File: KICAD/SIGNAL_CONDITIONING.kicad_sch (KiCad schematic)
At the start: 59 parts, among them U1 LM358, U4 LM358, U5 LM358, U6 LM358, U8 TLV9061

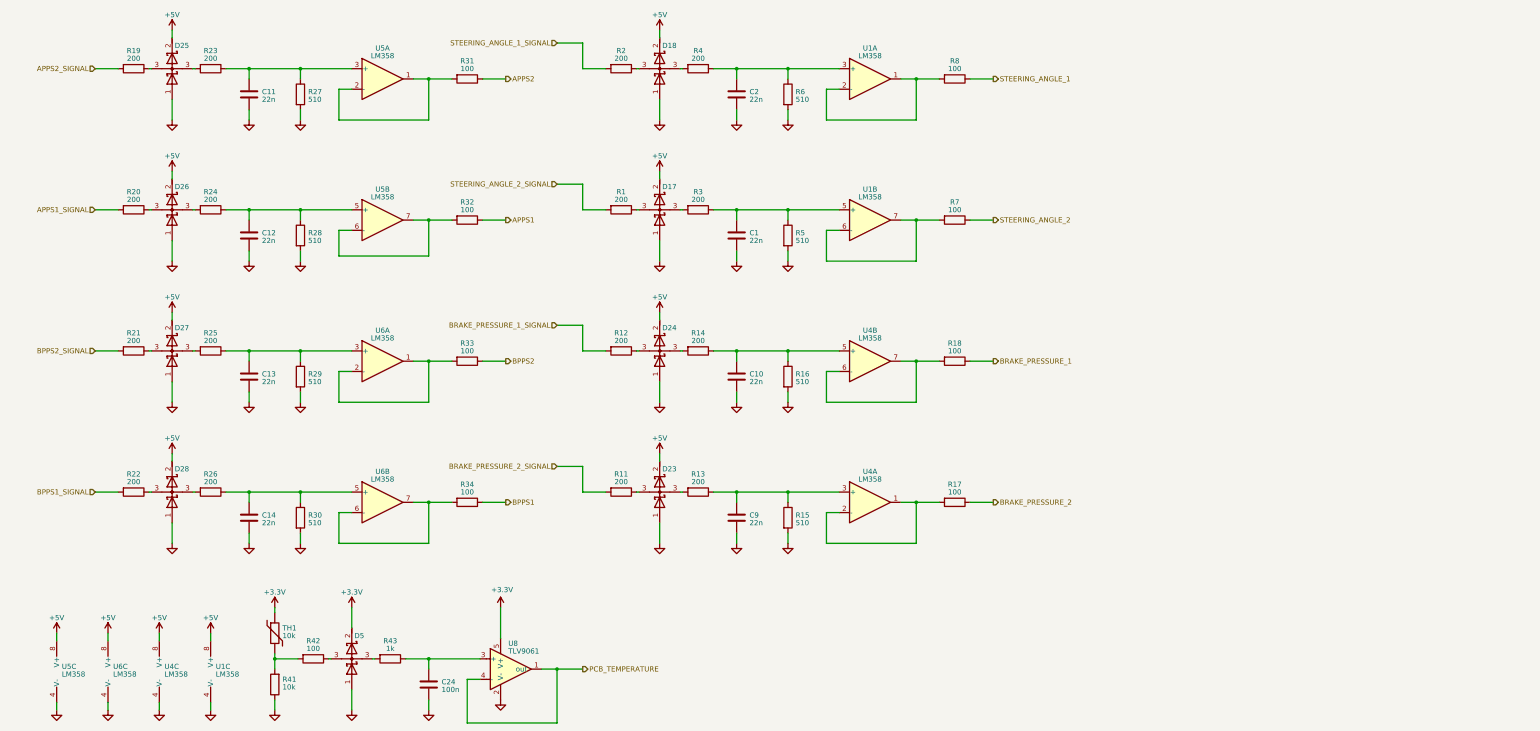
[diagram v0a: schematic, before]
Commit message: SIGNAL_CONDITIONING
Ändrat signal pins och dess output pins till ANALOG_SIGNAL_1 - ANALOG_1 osv för alla adnra siffror upp till 12. Pratade med VIktor ocg de vill att vi har tolv analoga inpus. Vi ska även döpa alla inuts till just ANALOG N (N-siffra) för att VMUn ska vara flexibel i framtiden och kunna användas för olika analoga sensorer utan att signalerna har angivna namn. Kopierade in fyra signal konditionerare till då det innan endast fanns 8 (eller 9) nu finns 12 (kanske 13)
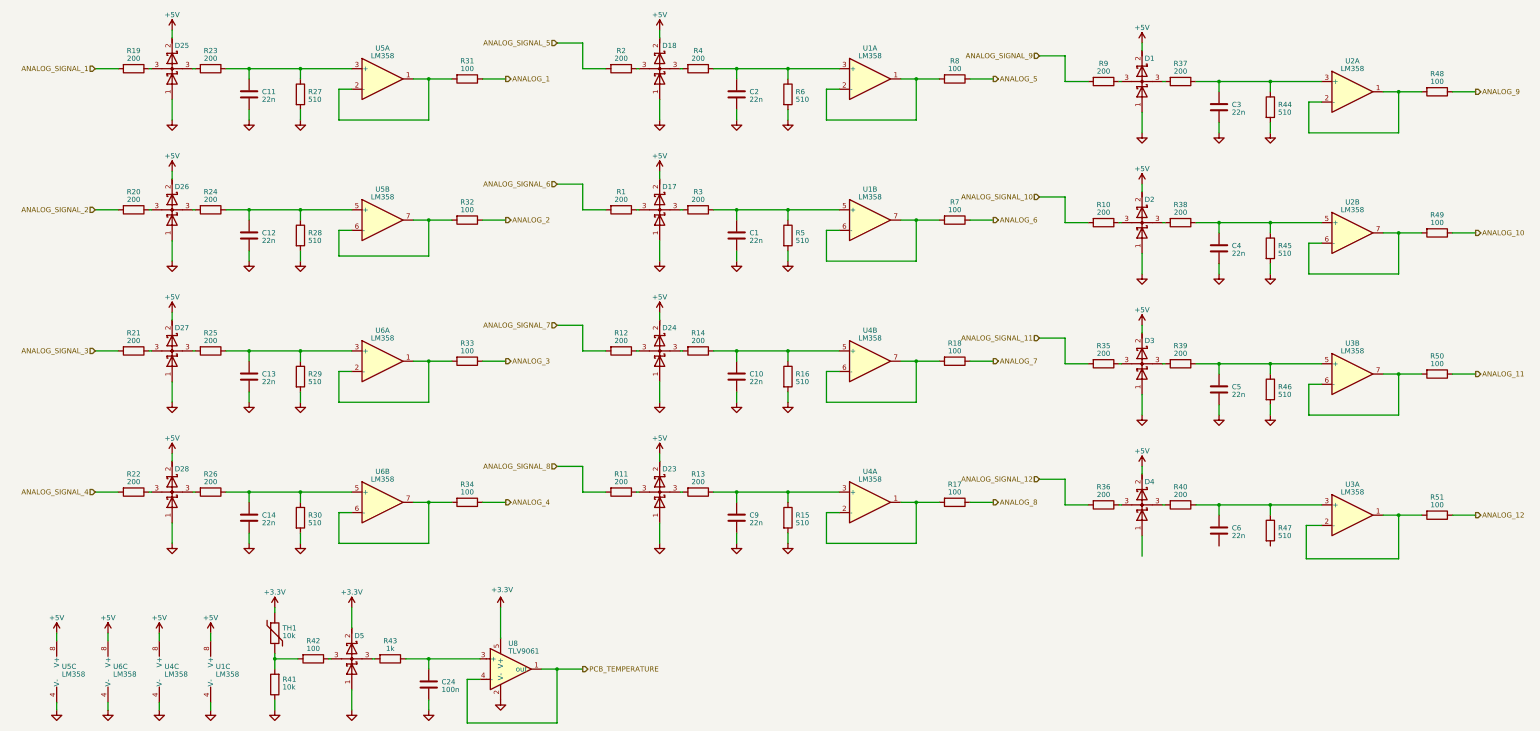
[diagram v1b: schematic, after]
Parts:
- added C3, C4, C5, C6: 22n, Capacitor_SMD:C_0603_1608Metric, symbol Device:C
- added D1, D2, D3, D4: D_Schottky_x2_Serial_AKC, Package_TO_SOT_SMD:SOT-23, symbol KTHFS:D_Schottky_x2_Serial_AKC
- added R10, R35, R36, R37, R38, R39, R40, R9: 200, Resistor_SMD:R_0603_1608Metric, symbol Device:R
- added R44, R45, R46, R47: 510, Resistor_SMD:R_0603_1608Metric, symbol Device:R
- added R48, R49, R50, R51: 100, Resistor_SMD:R_0603_1608Metric, symbol Device:R
- added U2, U3: LM358, Package_SO:SOIC-8_3.9x4.9mm_P1.27mm, symbol Amplifier_Operational:LM358
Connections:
- net +5V: now also D1.2 (K), D2.2 (K), D3.2 (K), D4.2 (K)
- net GND: now also C3.2, C4.2, C5.2, D1.1 (A), D2.1 (A), D3.1 (A), R44.2, R45.2, R46.2
- net APPS1 renamed ANALOG_2
- net APPS1_SIGNAL renamed ANALOG_SIGNAL_2
- net APPS2 renamed ANALOG_1
- net APPS2_SIGNAL renamed ANALOG_SIGNAL_1
- net BPPS1 renamed ANALOG_4
- net BPPS1_SIGNAL renamed ANALOG_SIGNAL_4
- net BPPS2 renamed ANALOG_3
- net BPPS2_SIGNAL renamed ANALOG_SIGNAL_3
- net BRAKE_PRESSURE_1 renamed ANALOG_7
- net BRAKE_PRESSURE_1_SIGNAL renamed ANALOG_SIGNAL_7
- net BRAKE_PRESSURE_2 renamed ANALOG_8
- net BRAKE_PRESSURE_2_SIGNAL renamed ANALOG_SIGNAL_8
- net STEERING_ANGLE_1 renamed ANALOG_5
- net STEERING_ANGLE_1_SIGNAL renamed ANALOG_SIGNAL_5
- net STEERING_ANGLE_2 renamed ANALOG_6
- net STEERING_ANGLE_2_SIGNAL renamed ANALOG_SIGNAL_6
- new net: D1.3 (common), R9.1
- new net: D1.3 (common), R37.2
- new net: C5.1, R39.1, R46.1, U3.5 (+)
- new net: D3.3 (common), R39.2
- new net: R49.2, U2.6 (-), U2.7
- new net: C4.1, R38.1, R45.1, U2.5 (+)
- new net: D2.3 (common), R38.2
- new net: R48.2, U2.1, U2.2 (-)
- new net: C3.1, R37.1, R44.1, U2.3 (+)
- new net: D3.3 (common), R35.1
- new net: R51.2, U3.1, U3.2 (-)
- new net: D4.3 (common), R36.1
- new net: C6.1, R40.1, R47.1, U3.3 (+)
- new net: D4.3 (common), R40.2
- new net: D2.3 (common), R10.1
- new net: R50.2, U3.6 (-), U3.7
- new net ANALOG_10: R49.1
- new net ANALOG_11: R50.1
- new net ANALOG_12: R51.1
- new net ANALOG_9: R48.1
- new net ANALOG_SIGNAL_10: R10.2
- new net ANALOG_SIGNAL_11: R35.2
- new net ANALOG_SIGNAL_12: R36.2
- new net ANALOG_SIGNAL_9: R9.2
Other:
- title: DRIVER CONTROL UNIT (DCU) -> VEHICLE MEASURING UNIT (VMU)

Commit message: Changed name on MCU
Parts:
- removed C3, C4, C5, C6: 22n, Capacitor_SMD:C_0603_1608Metric, symbol Device:C
- removed D1, D2, D3, D4: D_Schottky_x2_Serial_AKC, Package_TO_SOT_SMD:SOT-23, symbol KTHFS:D_Schottky_x2_Serial_AKC
- removed R10, R35, R36, R37, R38, R39, R40, R9: 200, Resistor_SMD:R_0603_1608Metric, symbol Device:R
- removed R44, R45, R46, R47: 510, Resistor_SMD:R_0603_1608Metric, symbol Device:R
- removed R48, R49, R50, R51: 100, Resistor_SMD:R_0603_1608Metric, symbol Device:R
- removed U2, U3: LM358, Package_SO:SOIC-8_3.9x4.9mm_P1.27mm, symbol Amplifier_Operational:LM358
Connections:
- net +3.3V: no longer D5.2 (K), U8.5 (V+)
- net +5V: no longer D17.2 (K), D18.2 (K), D23.2 (K), D24.2 (K), D25.2 (K), D26.2 (K), D27.2 (K), D28.2 (K)
- net GND: no longer D17.1 (A), D18.1 (A), D23.1 (A), D24.1 (A), D25.1 (A), D26.1 (A), D27.1 (A), D28.1 (A), D5.1 (A), U8.2 (V-)
- net PCB_TEMPERATURE: no longer U8.1 (out), U8.4 (-)
- net at R19.1: no longer D25.3 (common)
- net at R23.2: no longer D25.3 (common)
- net at R20.1: no longer D26.3 (common)
- net at R24.2: no longer D26.3 (common)
- net at R21.1: no longer D27.3 (common)
- net at R25.2: no longer D27.3 (common)
- net at R22.1: no longer D28.3 (common)
- net at R26.2: no longer D28.3 (common)
- net at R3.2: no longer D17.3 (common)
- net at R1.1: no longer D17.3 (common)
- net at R4.2: no longer D18.3 (common)
- net at R2.1: no longer D18.3 (common)
- net at R14.2: no longer D24.3 (common)
- net at R12.1: no longer D24.3 (common)
- net at R13.2: no longer D23.3 (common)
- net at R11.1: no longer D23.3 (common)
- net at C24.1, R43.1: no longer U8.3 (+)
- net at R43.2: no longer D5.3 (common)
- net at R42.1: no longer D5.3 (common)
- net ANALOG_1 renamed APPS2
- net ANALOG_2 renamed APPS1
- net ANALOG_3 renamed BPPS2
- net ANALOG_4 renamed BPPS1
- net ANALOG_5 renamed STEERING_ANGLE_1
- net ANALOG_6 renamed STEERING_ANGLE_2
- net ANALOG_7 renamed BRAKE_PRESSURE_1
- net ANALOG_8 renamed BRAKE_PRESSURE_2
- net ANALOG_SIGNAL_1 renamed APPS2_SIGNAL
- net ANALOG_SIGNAL_2 renamed APPS1_SIGNAL
- net ANALOG_SIGNAL_3 renamed BPPS2_SIGNAL
- net ANALOG_SIGNAL_4 renamed BPPS1_SIGNAL
- net ANALOG_SIGNAL_5 renamed STEERING_ANGLE_1_SIGNAL
- net ANALOG_SIGNAL_6 renamed STEERING_ANGLE_2_SIGNAL
- net ANALOG_SIGNAL_7 renamed BRAKE_PRESSURE_1_SIGNAL
- net ANALOG_SIGNAL_8 renamed BRAKE_PRESSURE_2_SIGNAL
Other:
- title: VEHICLE MEASURING UNIT (VMU) -> DRIVER CONTROL UNIT (DCU)
